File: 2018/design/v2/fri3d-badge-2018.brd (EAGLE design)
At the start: 80 x 60 mm, 138 parts

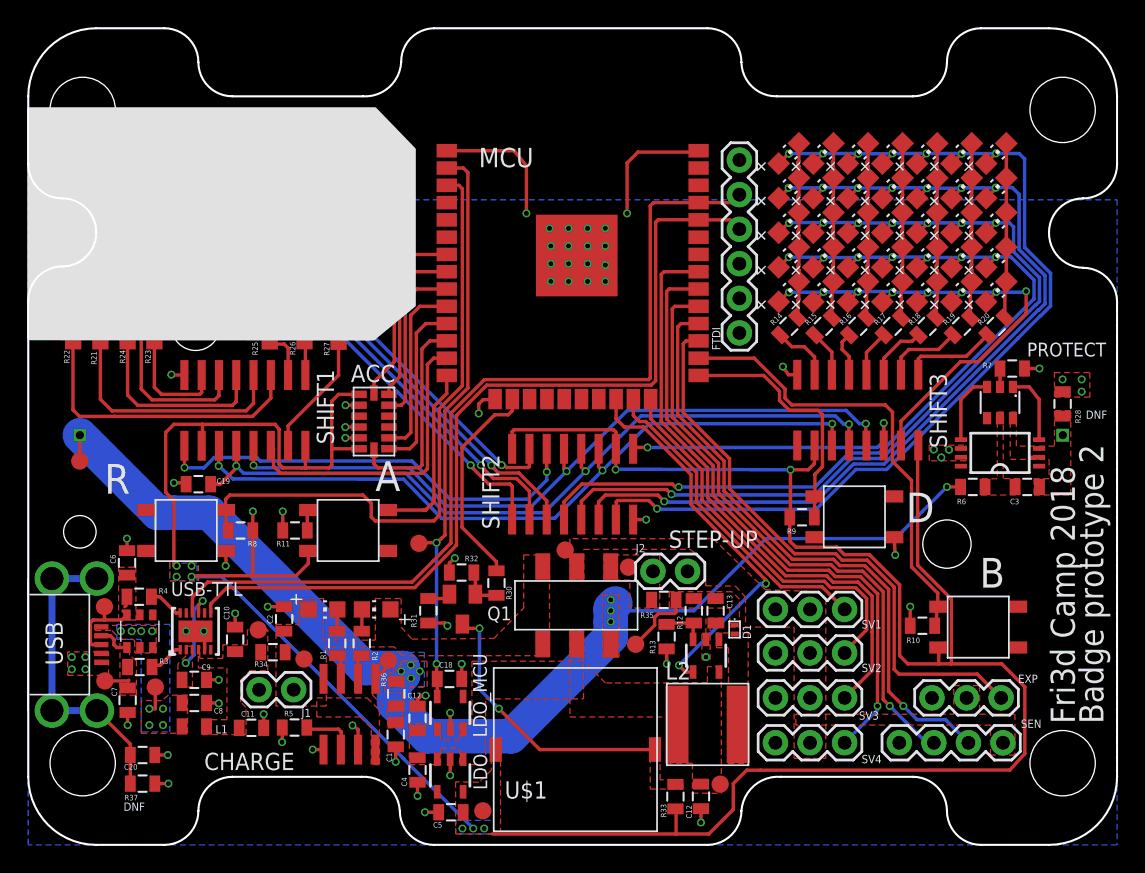
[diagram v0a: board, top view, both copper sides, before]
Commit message: further improved USB/ESD/FT traces
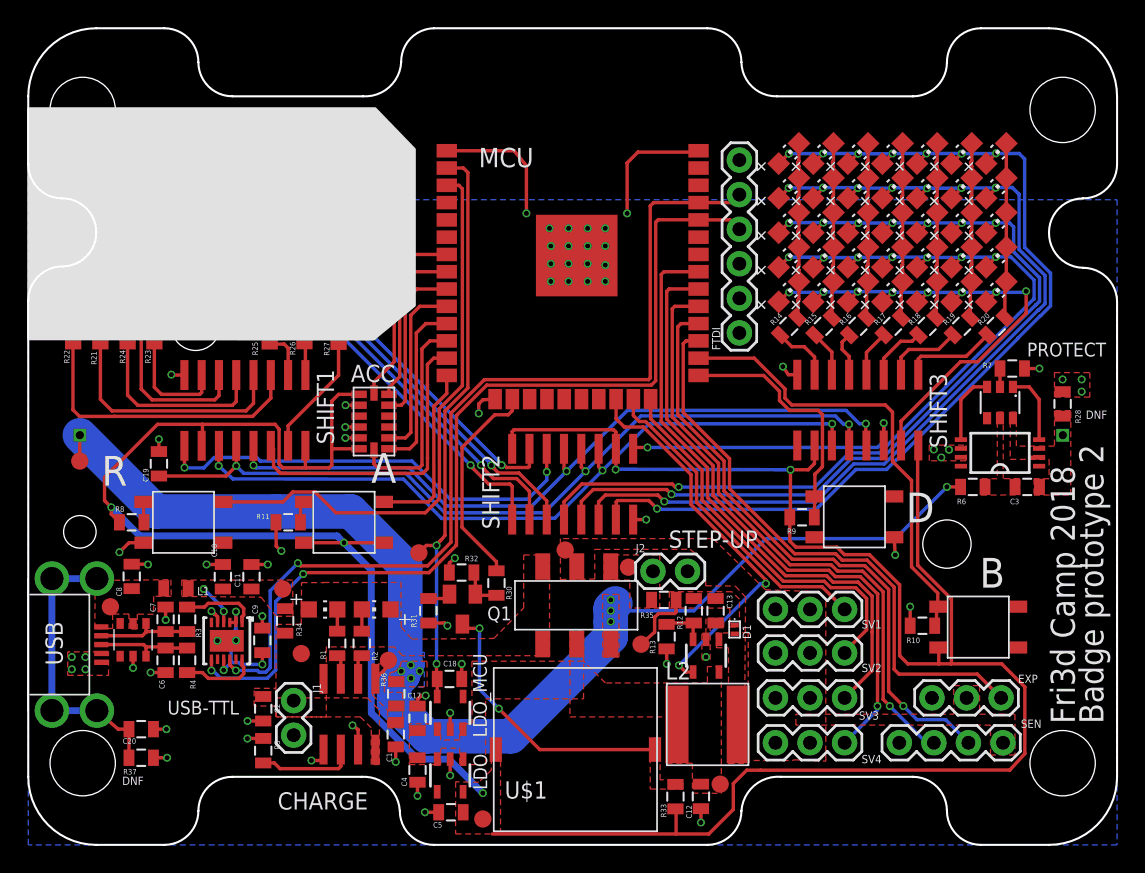
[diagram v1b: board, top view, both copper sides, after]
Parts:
- removed TP2, TP3: PTR1B1,27, testpad:B1,27
- moved C11 11.1 mm to (16.4, 19.7), turned to 90 degrees
- moved C8 10.4 mm to (7.60, 19.7), turned to 90 degrees
- moved L1 10.2 mm to (10.9, 18.9)
- moved R8 8.02 mm to (7.60, 23.7), turned to 180 degrees
- moved C6 7.70 mm to (10.1, 13.6), turned to 270 degrees
- moved C2 6.78 mm to (17.3, 10.0), turned to 270 degrees
- moved TP4 6.76 mm to (6.04, 17.5)
- moved C7 6.57 mm to (10.1, 16.6), turned to 90 degrees
- moved R4 5.85 mm to (11.7, 13.6), turned to 270 degrees
- moved C9 5.78 mm to (17.2, 15.0), turned to 90 degrees
- moved R3 4.94 mm to (11.7, 16.6), turned to 90 degrees
- moved C10 4.69 mm to (14.3, 19.7)
- moved TP1 3.50 mm to (18.7, 18.8)
- moved C19 3.26 mm to (9.60, 28.0), turned to 270 degrees
- moved R5 2.86 mm to (17.3, 6.92), turned to 270 degrees
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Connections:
- net D+: no longer TP2.TP
- net D-: no longer TP3.TP
- net GND: now also U$2.2
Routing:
- net RX: track 63.9 -> 69.4 mm, vias 0 -> 2
- net GND: track 65.8 -> 70.3 mm, vias 67 -> 69
- net 3V3: track 206.6 -> 211.0 mm, vias 10 -> 5
- net N$6: track 6.14 -> 10.1 mm, vias 2 -> 3
- net VBAT: track 88.5 -> 92.4 mm
- net LEDS_RCK: track 57.0 -> 60.6 mm
- net N$10: track 3.98 -> 7.18 mm
- net N$5: track 2.60 -> 5.59 mm
- net USB-FILTERED: track 0.14 -> 3.07 mm, vias 0 -> 2
- net N$3: track 2.59 -> 5.51 mm
- net D-: track 4.58 -> 7.07 mm
- net TX: track 66.6 -> 69.1 mm, vias 0 -> 2
- net USB-RAW: track 2.21 -> 0.00 mm, vias 8 -> 0
- net RESET: track 45.7 -> 43.9 mm
- net N$23: track 22.7 -> 21.3 mm
- removed copper zone on layer 16, net 3V3
- removed copper zone on layer 1, net D+
- removed copper zone on layer 1, net D-
- removed copper zone on layer 1, net N$6
- removed copper zone on layer 16, net USB-RAW

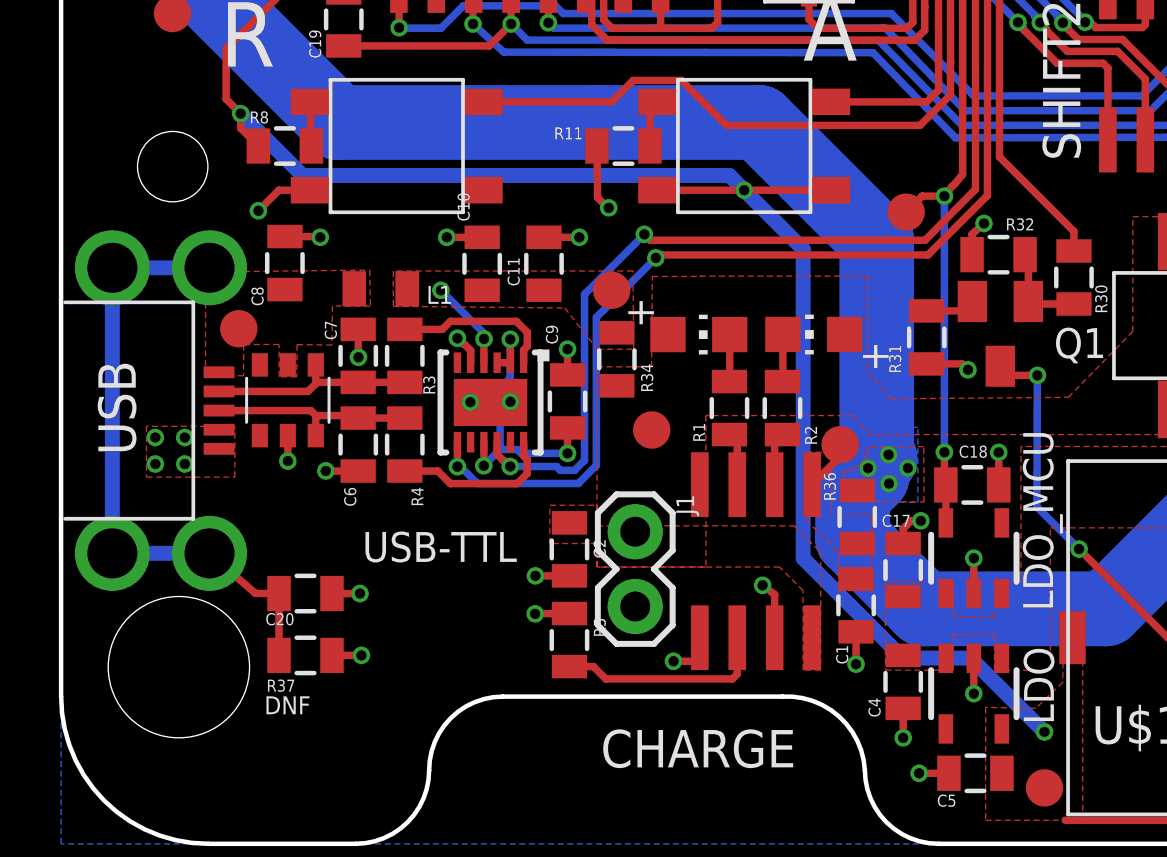
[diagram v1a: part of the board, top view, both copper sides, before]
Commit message: redid USB intake again, uncrossing lines at conn
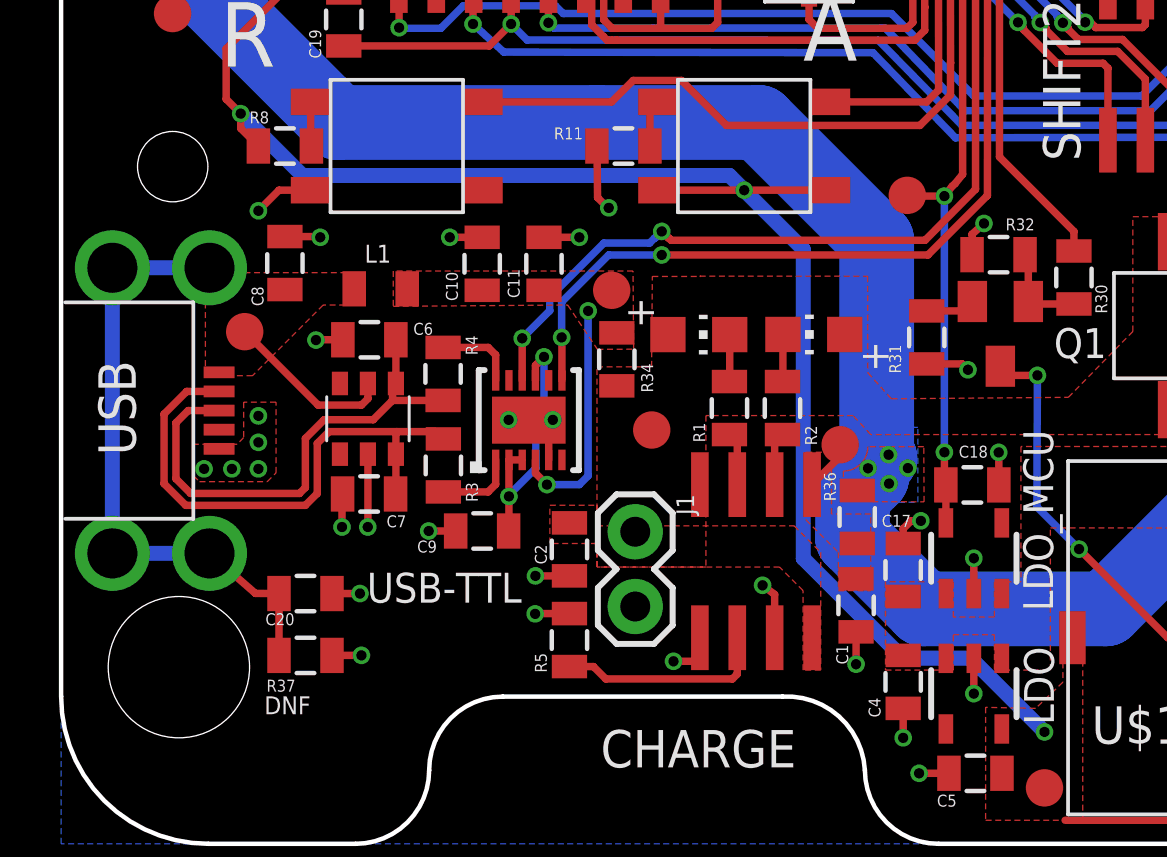
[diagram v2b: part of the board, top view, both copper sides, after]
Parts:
- moved C9 5.27 mm to (14.3, 10.6), turned to 180 degrees
- moved C7 4.70 mm to (10.5, 11.9), turned to 180 degrees
- moved R3 3.94 mm to (13.0, 12.9), turned to 270 degrees
- moved C6 3.58 mm to (10.5, 17.1), turned to 180 degrees
- moved U$2 2.79 mm to (10.4, 14.4)
- moved R4 2.73 mm to (13.0, 16.0), turned to 90 degrees
- moved USB-TTL 1.43 mm to (15.9, 14.4), turned to 90 degrees
- moved TP9 0.57 mm to (28.7, 22.0)
- moved TP4 0.22 mm to (6.24, 17.4)
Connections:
- net D+: now also U$2.4; no longer U$2.3
- net D-: now also U$2.3; no longer U$2.4
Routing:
- net D-: track 7.07 -> 18.6 mm
- net D+: track 7.10 -> 17.2 mm
- net RX: track 69.4 -> 62.0 mm
- net USB-RAW: track 0.00 -> 5.82 mm
- net USB-FILTERED: track 3.07 -> 8.13 mm
- net TX: track 69.1 -> 64.2 mm
- net N$5: track 5.59 -> 2.76 mm
- net N$3: track 5.51 -> 2.71 mm
- net GND: track 70.3 -> 72.6 mm
- net N$6: track 10.1 -> 9.02 mm, vias 3 -> 2

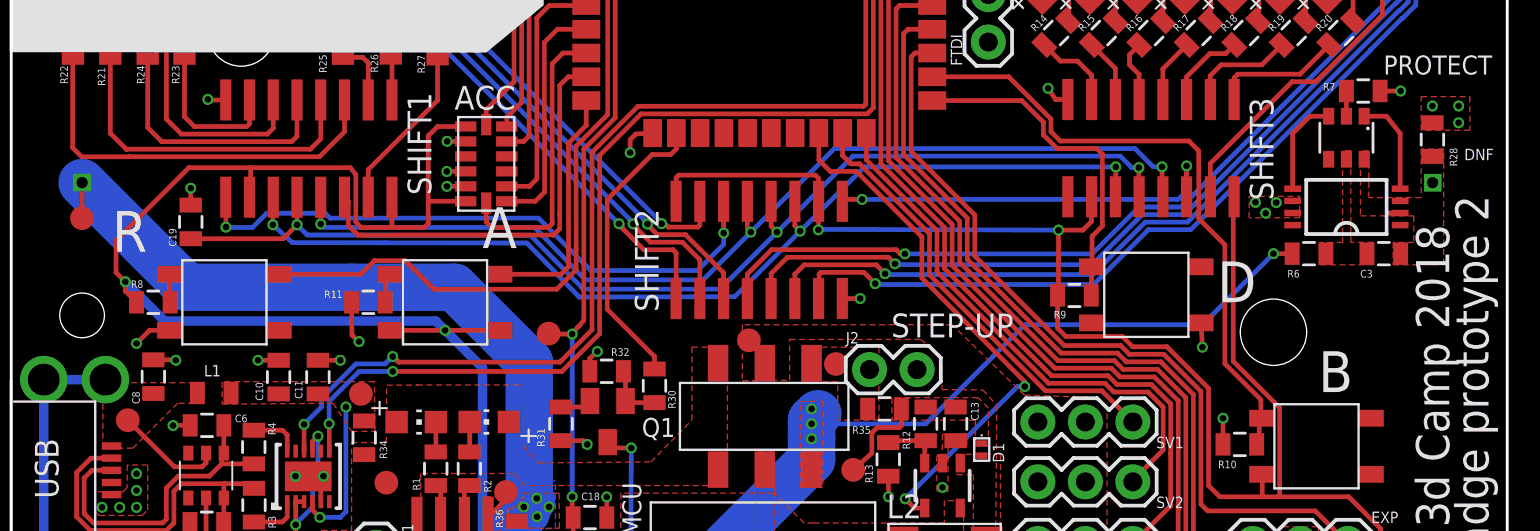
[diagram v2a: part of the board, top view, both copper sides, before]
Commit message: swapped position of buttons R and A
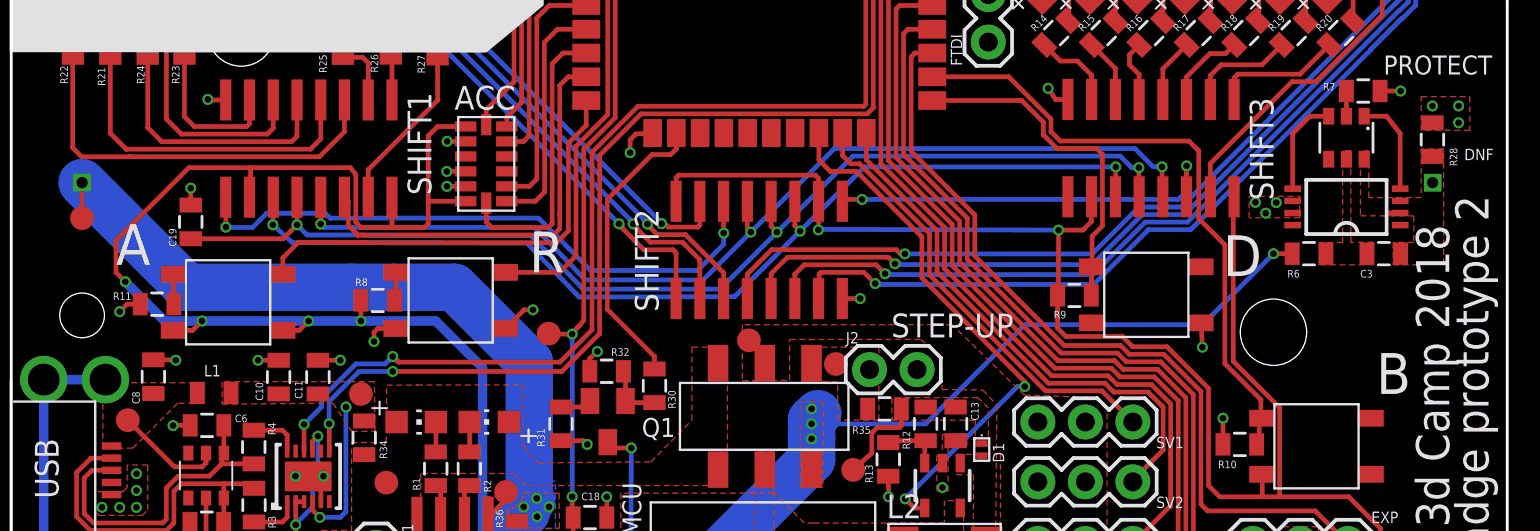
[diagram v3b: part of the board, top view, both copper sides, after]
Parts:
- moved R 12.1 mm to (23.5, 23.8)
- moved R8 12.0 mm to (19.6, 23.8)
- moved A 11.6 mm to (11.6, 23.7)
- moved R11 11.3 mm to (7.80, 23.6)
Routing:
- net RESET: track 43.9 -> 29.6 mm
- net BUTTON-B: track 14.7 -> 25.7 mm
- net 3V3: track 211.0 -> 208.1 mm, vias 5 -> 7
- net GND: track 72.6 -> 73.2 mm, vias 69 -> 70
